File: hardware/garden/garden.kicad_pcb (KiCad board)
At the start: 4 copper layers, 53.3 x 83.8 mm, 53 parts, among them J1 CONN_01X40, J2 CONN_01X08, J3 CONN_01X06, J4 CONN_01X10, J5 CONN_01X08, J7 Micro_SD_Card_CD, J8 CONN_01X13, J9 CONN_01X06, M1 ESP-11, M2 CONN_01X01, M3 CONN_01X01, M4 CONN_01X01, M5 CONN_01X01, P1 USB_OTG, Q1 Q_NMOS_GSD, SW1 RESET, SW2 BOOT, U1 AZ1117-3.3, U2 STM32F745ZETx, U3 IS42S16160G, Y1 12MHz

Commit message: Designed garden controller
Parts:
- added C17: 1uF, Capacitor_SMD:C_0805_2012Metric_Pad1.15x1.40mm_HandSolder, F.Cu at (122.0, 98.0)
- added C18: 0.1uF, Capacitor_SMD:C_0805_2012Metric_Pad1.15x1.40mm_HandSolder, F.Cu at (118.9, 106.0)
- added C19: 0.1uF, Capacitor_SMD:C_0805_2012Metric_Pad1.15x1.40mm_HandSolder, F.Cu at (118.7, 111.1)
- added C20: 0.1uF, Capacitor_SMD:C_0805_2012Metric_Pad1.15x1.40mm_HandSolder, F.Cu at (118.6, 117.5)
- added C21: 220uF, Capacitor_THT:CP_Radial_D8.0mm_P3.50mm, F.Cu at (137.6, 77.7)
- added C22: 220uF, Capacitor_THT:CP_Radial_D8.0mm_P3.50mm, F.Cu at (114.0, 136.0)
- added C23: 22uF, Capacitor_THT:CP_Radial_D6.3mm_P2.50mm, F.Cu at (75.3, 68.3)
- added D7: D_Schottky, Diode_SMD:D_1206_3216Metric_Pad1.42x1.75mm_HandSolder, F.Cu at (147.8, 66.0)
- added J10: CONN_01X10, Connector_PinHeader_2.54mm:PinHeader_1x10_P2.54mm_Vertical, F.Cu at (61.8, 104.6)
- added J6: CONN_01X02, TerminalBlock_Phoenix:TerminalBlock_Phoenix_MKDS-3-2-5.08_1x02_P5.08mm_Horizontal, F.Cu at (148.0, 126.2)
- added Q2: Q_NMOS_GDS, Package_TO_SOT_THT:TO-220-3_Vertical, F.Cu at (128.7, 101.8)
- added Q3: Q_NMOS_GDS, Package_TO_SOT_THT:TO-220-3_Vertical, F.Cu at (128.7, 107.1)
- added R11: 1kR, Resistor_SMD:R_0805_2012Metric_Pad1.15x1.40mm_HandSolder, F.Cu at (94.2, 110.7)
- added R12: 1kR, Resistor_SMD:R_0805_2012Metric_Pad1.15x1.40mm_HandSolder, F.Cu at (94.2, 114.4)
- added U4: MIC4427, Package_SO:SOIC-8_3.9x4.9mm_P1.27mm, F.Cu at (122.0, 93.5)
- added U5: INA193, Package_TO_SOT_SMD:SOT-23-5, F.Cu at (121.9, 106.1)
- added U6: INA193, Package_TO_SOT_SMD:SOT-23-5, F.Cu at (121.9, 111.1)
- added U7: TEC2-1215WI, Converter_DCDC:Converter_DCDC_TRACO_TMR-xxxx_THT, F.Cu at (126.2, 143.7)
- added U8: INA193, Package_TO_SOT_SMD:SOT-23-5, F.Cu at (121.9, 117.4)
- C14: footprint Capacitors_SMD:C_0805 -> Capacitor_SMD:C_0805_2012Metric_Pad1.15x1.40mm_HandSolder
- C15, C16: value 10uF -> 0.1uF; footprint Capacitors_SMD:C_0805 -> Capacitor_SMD:C_0805_2012Metric_Pad1.15x1.40mm_HandSolder
- J1: value CONN_01X40 -> CONN_01X04; footprint ER-CON40HB-2:ER-CON40HB-2 -> Connector_JST:JST_PH_B4B-PH-SM4-TB_1x04-1MP_P2.00mm_Vertical
- J2, J5: value CONN_01X08 -> CONN_01X02; footprint Pin_Headers:Pin_Header_Straight_1x08_Pitch2.54mm -> TerminalBlock_Phoenix:TerminalBlock_Phoenix_MKDS-3-2-5.08_1x02_P5.08mm_Horizontal
- J3: value CONN_01X06 -> CONN_01X04; footprint Pin_Headers:Pin_Header_Straight_1x06_Pitch2.54mm -> Connector_JST:JST_PH_B4B-PH-SM4-TB_1x04-1MP_P2.00mm_Vertical
- J4: value CONN_01X10 -> CONN_01X02; footprint Connector_PinHeader_2.54mm:PinHeader_1x10_P2.54mm_Vertical -> TerminalBlock_Phoenix:TerminalBlock_Phoenix_MKDS-3-2-5.08_1x02_P5.08mm_Horizontal
- J7: value Micro_SD_Card_CD -> CONN_01X04; footprint Amphenol:Amphenol_1140084168 -> TerminalBlock_Phoenix:TerminalBlock_Phoenix_MPT-0,5-4-2.54_1x04_P2.54mm_Horizontal
- J8: value CONN_01X13 -> CONN_01X04; footprint Pin_Headers:Pin_Header_Straight_1x13_Pitch2.54mm -> TerminalBlock_Phoenix:TerminalBlock_Phoenix_MPT-0,5-4-2.54_1x04_P2.54mm_Horizontal
- M2, M3, M4, M5: footprint Mechanical:M2_HOLE -> MountingHole:MountingHole_6.4mm_M6
- R1, R4: value 10KR -> 10mR; footprint Resistors_SMD:R_0805 -> Resistor_SMD:R_1206_3216Metric_Pad1.42x1.75mm_HandSolder
- R5: value 10KR -> 1kR; footprint Resistors_SMD:R_0805 -> Resistor_SMD:R_0805_2012Metric_Pad1.15x1.40mm_HandSolder
- R6: value 10KR -> 6.8R; footprint Resistors_SMD:R_0805 -> Resistor_SMD:R_0805_2012Metric_Pad1.15x1.40mm_HandSolder
- U1: footprint SOT-223 -> Package_TO_SOT_SMD:SOT-223
- U3: value IS42S16160G -> R-78B5.0-2.0; footprint TSOPII:TSOPII-54_10.16x22.22mm-Pitch0.8mm -> Converter_DCDC:Converter_DCDC_RECOM_R-78B-2.0_THT
- moved J1 85.4 mm to (78.4, 82.7), turned to 90 degrees
- moved J7 70.5 mm to (87.0, 144.5), turned to 0 degrees
- moved C14 60.9 mm to (106.4, 76.2)
- moved U3 54.5 mm to (150.4, 75.9), turned to 180 degrees
- moved J3 50.6 mm to (65.5, 82.7), turned to 90 degrees
- moved J2 49.6 mm to (148.0, 82.7), turned to 270 degrees
- moved R6 49.6 mm to (147.8, 122.0)
- moved R1 43.0 mm to (147.4, 92.5)
- moved C15 40.2 mm to (94.2, 105.7)
- moved M2 38.5 mm to (63.8, 56.6)
- moved M5 37.6 mm to (63.2, 141.9)
- moved J8 36.6 mm to (73.9, 144.5), turned to 0 degrees
- moved Q1 34.8 mm to (115.3, 65.7), turned to 90 degrees
- moved P1 30.3 mm to (132.8, 52.3), turned to 270 degrees
- moved C3 29.9 mm to (81.9, 99.3), turned to 90 degrees
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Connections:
- net /PA9 renamed /Vusb
- C16 pad 1: +3V3 -> +12V
- J1 pad 2: /LCD_BL -> /VD_RX
- J1 pad 3: GND -> /VD_TX
- J1 pad 4: /TOUCH_WAKE -> (no net)
- J2 pad 1: Net-(J2-Pad1) -> +12V
- J2 pad 2: +3V3 -> GND
- J3 pad 1: /PA0 -> GND
- J3 pad 2: /PA1 -> /VD_TX
- J3 pad 3: /PA2 -> /VD_RX
- J3 pad 4: /PA3 -> (no net)
- J4 pad 1: /PA8 -> Net-(J4-Pad1)
- J4 pad 2: /PC9 -> Net-(J4-Pad2)
- J5 pad 1: /PG7 -> Net-(J5-Pad1)
- J5 pad 2: /PC6 -> Net-(J5-Pad2)
- J7 pad 1: Net-(J7-Pad1) -> +3V3
- J7 pad 2: /SD_CS -> /SDA
- J7 pad 3: /SD_MOSI -> /SCL
- J7 pad 4: +3V3 -> GND
- J8 pad 2: GND -> /SDA
- J8 pad 3: /~LCD_CS -> /SCL
- J8 pad 4: /~LCD_RD -> GND
- M2 pad 1: Net-(M2-Pad1) -> (no net)
- M3 pad 1: Net-(M3-Pad1) -> (no net)
- M4 pad 1: Net-(M4-Pad1) -> (no net)
- M5 pad 1: Net-(M5-Pad1) -> (no net)
- P1 pad 4: Net-(P1-Pad4) -> (no net)
- R1 pad 1: +3V3 -> +12V
- R1 pad 2: /SD_CD -> Net-(J4-Pad1)
- R4 pad 1: +3V3 -> +12V
- R4 pad 2: /TOUCH_SDA -> Net-(J5-Pad1)
- R5 pad 1: +3V3 -> Net-(R5-Pad1)
- R5 pad 2: /TOUCH_SCL -> /PRESSURE_PWR
- R6 pad 1: +3V3 -> Net-(J6-Pad1)
- R6 pad 2: /SD_MISO -> Net-(R6-Pad2)
- U2 pad 1: /SD_SCLK -> (no net)
- U2 pad 10: /A0 -> /PF0
- U2 pad 100: /PA8 -> (no net)
- U2 pad 102: /PA10 -> (no net)
- U2 pad 11: /A1 -> /PF1
- U2 pad 110: /PA15 -> (no net)
- U2 pad 111: /PC10 -> (no net)
- U2 pad 112: /PC11 -> (no net)
- U2 pad 113: /PC12 -> (no net)
- U2 pad 114: /D2 -> (no net)
- U2 pad 115: /D3 -> (no net)
- U2 pad 116: Net-(U2-Pad116) -> (no net)
- U2 pad 117: Net-(U2-Pad117) -> (no net)
- U2 pad 118: /~LCD_RD -> (no net)
- U2 pad 119: /~LCD_WR -> (no net)
- U2 pad 12: /A2 -> /PF2
- U2 pad 122: /LCD_TE -> (no net)
- U2 pad 123: /~LCD_CS -> (no net)
- U2 pad 13: /A3 -> (no net)
- U2 pad 132: /SDNCAS -> (no net)
- U2 pad 139: Net-(U2-Pad139) -> (no net)
- U2 pad 14: /A4 -> (no net)
- U2 pad 140: Net-(U2-Pad140) -> (no net)
- U2 pad 141: /NBL0 -> /VD_RX
- U2 pad 142: /NBL1 -> /VD_TX
- U2 pad 15: /A5 -> (no net)
- U2 pad 18: Net-(U2-Pad18) -> (no net)
- U2 pad 19: Net-(U2-Pad19) -> (no net)
- U2 pad 2: /SD_CD -> (no net)
- U2 pad 20: Net-(U2-Pad20) -> (no net)
- U2 pad 21: Net-(U2-Pad21) -> (no net)
- U2 pad 22: Net-(U2-Pad22) -> (no net)
- U2 pad 26: /SDNWE -> (no net)
- U2 pad 27: Net-(U2-Pad27) -> (no net)
- U2 pad 28: /SDNE0 -> (no net)
- U2 pad 29: /SDCKE0 -> (no net)
- U2 pad 3: /SD_CS -> (no net)
- U2 pad 34: /PA0 -> (no net)
- U2 pad 4: /SD_MISO -> (no net)
- U2 pad 40: /PA4 -> (no net)
- U2 pad 41: /PA5 -> (no net)
- U2 pad 42: Net-(U2-Pad42) -> (no net)
- U2 pad 43: /PA7 -> (no net)
- U2 pad 44: Net-(U2-Pad44) -> (no net)
- U2 pad 45: Net-(U2-Pad45) -> /PRESSURE_CUR
- U2 pad 46: Net-(U2-Pad46) -> /SW1_CUR
- U2 pad 47: Net-(U2-Pad47) -> /SW0_CUR
- U2 pad 48: Net-(U2-Pad48) -> (no net)
- U2 pad 49: /SDNRAS -> (no net)
- U2 pad 5: /SD_MOSI -> (no net)
- U2 pad 50: /A6 -> (no net)
- U2 pad 53: /A7 -> (no net)
- U2 pad 54: /A8 -> /SCL
- U2 pad 55: /A9 -> /SDA
- U2 pad 56: /A10 -> (no net)
- U2 pad 57: /A11 -> (no net)
- U2 pad 58: /D4 -> (no net)
- U2 pad 59: /D5 -> (no net)
- U2 pad 60: /D6 -> (no net)
- U2 pad 63: /D7 -> (no net)
- U2 pad 64: /D8 -> (no net)
- U2 pad 65: /D9 -> (no net)
- U2 pad 66: /D10 -> (no net)
- U2 pad 67: /D11 -> (no net)
- U2 pad 68: /D12 -> (no net)
- U2 pad 69: /TOUCH_SCL -> (no net)
- U2 pad 7: Net-(U2-Pad7) -> (no net)
- U2 pad 70: /TOUCH_SDA -> /PRESSURE_PWR
- U2 pad 73: /TOUCH_INT -> (no net)
- U2 pad 74: /TOUCH_WAKE -> (no net)
- U2 pad 75: /TOUCH_RESET -> (no net)
- U2 pad 76: /LCD_BL -> (no net)
- U2 pad 77: /D13 -> (no net)
- U2 pad 78: /D14 -> (no net)
- U2 pad 79: /D15 -> (no net)
- U2 pad 8: Net-(U2-Pad8) -> (no net)
- U2 pad 80: /PD11 -> (no net)
- U2 pad 81: /PD12 -> (no net)
- U2 pad 82: /PD13 -> (no net)
- U2 pad 85: /D0 -> (no net)
- U2 pad 86: /D1 -> (no net)
- U2 pad 87: /A12 -> (no net)
- U2 pad 88: Net-(U2-Pad88) -> (no net)
- U2 pad 89: /BA0 -> (no net)
- U2 pad 9: Net-(U2-Pad9) -> (no net)
- U2 pad 90: /BA1 -> (no net)
- U2 pad 91: /PG6 -> (no net)
- U2 pad 92: /PG7 -> /SW1_SIG
- U2 pad 93: /SDCLK -> /SW0_SIG
- U2 pad 96: /PC6 -> (no net)
- U2 pad 97: /PC7 -> (no net)
- U2 pad 98: /PC8 -> (no net)
- U2 pad 99: /PC9 -> (no net)
- U3 pad 1: +3V3 -> +12V
- U3 pad 2: /D0 -> GND
- U3 pad 3: +3V3 -> Net-(D7-Pad2)
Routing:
- net +3V3: track 159.8 -> 354.3 mm, vias 33 -> 16
- net GND: track 145.8 -> 297.4 mm, vias 41 -> 34
- net +12V: track 0.00 -> 126.2 mm, vias 0 -> 10
- net VCC: track 116.1 -> 11.7 mm, vias 1 -> 0
- net /~LCD_RD: track 74.5 -> 0.00 mm, vias 4 -> 0
- net /~LCD_WR: track 74.3 -> 0.00 mm, vias 4 -> 0
- net /LCD_TE: track 74.2 -> 0.00 mm, vias 4 -> 0
- net /~LCD_CS: track 73.3 -> 0.00 mm, vias 4 -> 0
- net /SCL: track 0.00 -> 72.5 mm, vias 0 -> 2
- net /SDA: track 0.00 -> 70.1 mm, vias 0 -> 5
- net /D2: track 62.1 -> 0.00 mm, vias 4 -> 0
- net /D3: track 60.2 -> 0.00 mm, vias 4 -> 0
- net /TOUCH_SCL: track 58.1 -> 0.00 mm, vias 2 -> 0
- net /TOUCH_SDA: track 57.6 -> 0.00 mm, vias 2 -> 0
- net /D0: track 52.2 -> 0.00 mm, vias 4 -> 0
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- added copper zone on B.Cu, net +12V
- added copper zone on B.Cu, net +3V3
- added copper zone on B.Cu, net GND
- removed copper zone on F.Cu, net +3V3
- removed copper zone on VDD, net +3V3
- removed copper zone on GND, net GND
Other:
- board size 53.3 x 83.8 mm -> 99.7 x 99.7 mm
- copper layers 4 -> 2
- rule via_min_size: 0.4 -> 0.45
- board text added: "+"
- board text added: "-"
- board text added: "12V"
- board text added: "I2C0"
- board text added: "I2C1"
- board text added: "PA1"
- board text added: "PA2"
- board text added: "PA3"
- board text added: "PF0"
- board text added: "PF1"
- board text added: "PF2"
- board text added: "Pressure IN"
- board text added: "Pump OUT"
- board text added: "SCL"
- board text added: "SDA"
- board text added: "SW1 OUT"
- board text added: "Solar Power IN"
- board text added: "VE.Direct"
- board text added: "WiredHut Garden Controller Rev 1"
- board text removed: "A0"
- board text removed: "A1"
- board text removed: "A2"
- board text removed: "A3"
- board text removed: "A4"
- board text removed: "A5"
- board text removed: "D0"
- board text removed: "D1"
- board text removed: "D10"
- board text removed: "D11"
- board text removed: "D12"
- board text removed: "D13"
- board text removed: "D14"
- board text removed: "D15"
- board text removed: "D2"
- board text removed: "D20"
- board text removed: "D21"
- board text removed: "D22"
- board text removed: "D23"
- board text removed: "D24"
- board text removed: "D25"
- board text removed: "D26"
- board text removed: "D27"
- board text removed: "D28"
- board text removed: "D3"
- board text removed: "D4"
- board text removed: "D5"
- board text removed: "D6"
- board text removed: "D7"
- board text removed: "D8"
- board text removed: "D9"
- board text removed: "Ostrich"
- board text removed: "Rev 2"
- board text removed: "VCC"
- board text removed: "Vcc"
- board text removed: "~RST"

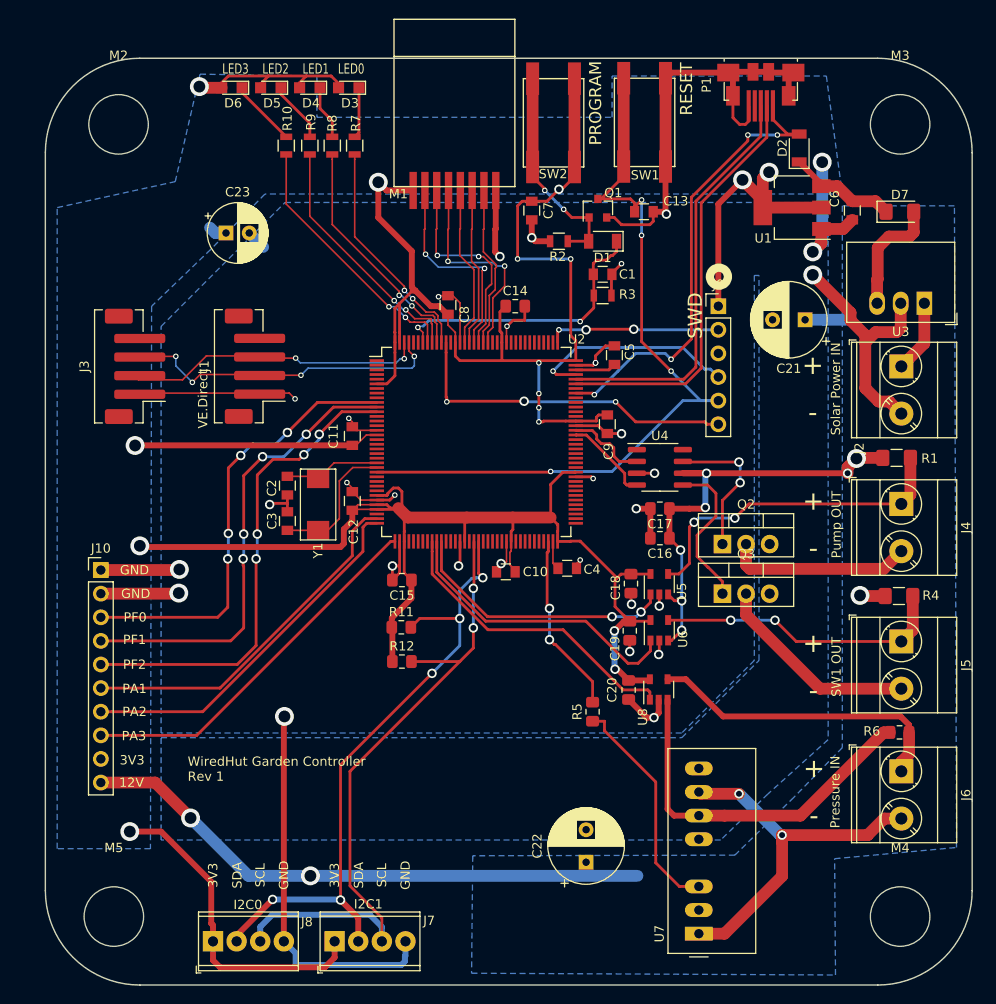
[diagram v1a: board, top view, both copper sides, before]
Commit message: Updated garden controller with test points and back emf diodes
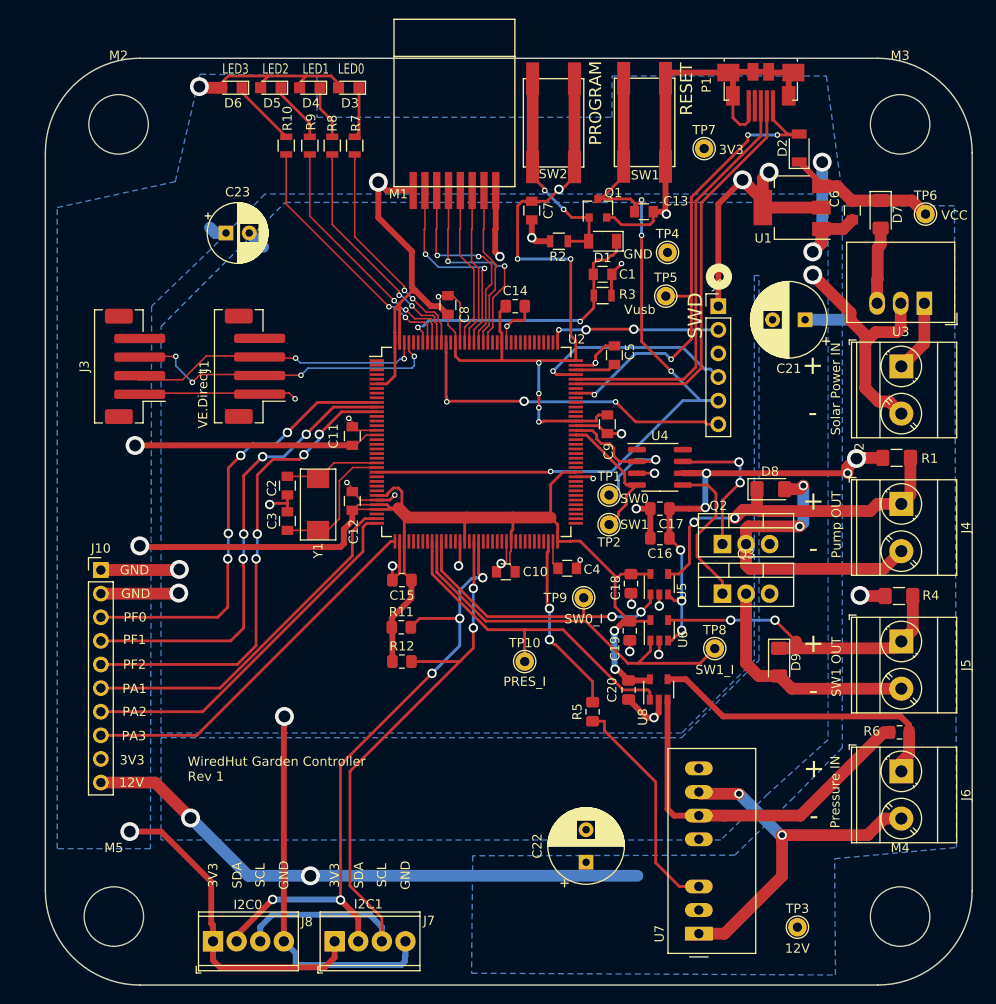
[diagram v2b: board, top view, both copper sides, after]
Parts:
- added D8: D_Schottky, Diode_SMD:D_1206_3216Metric_Pad1.42x1.75mm_HandSolder, F.Cu at (133.9, 95.9)
- added D9: D_Schottky, Diode_SMD:D_1206_3216Metric_Pad1.42x1.75mm_HandSolder, F.Cu at (134.8, 114.5)
- added TP1: TestPoint, TestPoint:TestPoint_THTPad_D2.0mm_Drill1.0mm, F.Cu at (116.5, 96.5)
- added TP10: TestPoint, TestPoint:TestPoint_THTPad_D2.0mm_Drill1.0mm, F.Cu at (107.4, 114.4)
- added TP2: TestPoint, TestPoint:TestPoint_THTPad_D2.0mm_Drill1.0mm, F.Cu at (116.5, 99.7)
- added TP3: TestPoint, TestPoint:TestPoint_THTPad_D2.0mm_Drill1.0mm, F.Cu at (136.8, 143.0)
- added TP4: TestPoint, TestPoint:TestPoint_THTPad_D2.0mm_Drill1.0mm, F.Cu at (122.8, 70.4)
- added TP5: TestPoint, TestPoint:TestPoint_THTPad_D2.0mm_Drill1.0mm, F.Cu at (122.6, 75.1)
- added TP6: TestPoint, TestPoint:TestPoint_THTPad_D2.0mm_Drill1.0mm, F.Cu at (150.6, 66.3)
- added TP7: TestPoint, TestPoint:TestPoint_THTPad_D2.0mm_Drill1.0mm, F.Cu at (126.7, 59.2)
- added TP8: TestPoint, TestPoint:TestPoint_THTPad_D2.0mm_Drill1.0mm, F.Cu at (127.9, 113.0)
- added TP9: TestPoint, TestPoint:TestPoint_THTPad_D2.0mm_Drill1.0mm, F.Cu at (113.8, 107.6)
- moved D7 2.09 mm to (145.7, 66.3), turned to 270 degrees
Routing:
- net Net-(D8-Pad2): track 19.9 -> 34.2 mm, vias 0 -> 2
- net /SW0_SIG: track 8.74 -> 18.3 mm, vias 0 -> 1
- net /SW1_CUR: track 32.0 -> 40.9 mm
- net /SW1_SIG: track 9.41 -> 14.9 mm
- net Net-(D7-Pad2): track 12.8 -> 8.23 mm
- net VCC: track 11.7 -> 16.1 mm
- net /PRESSURE_CUR: track 33.0 -> 36.4 mm
- net Net-(D9-Pad2): track 22.3 -> 25.3 mm
- net Net-(D9-Pad1): track 31.4 -> 34.4 mm
- net /Vusb: track 50.5 -> 53.3 mm
- net Net-(D8-Pad1): track 35.9 -> 38.2 mm
- net /SW0_CUR: track 29.2 -> 31.3 mm
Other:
- board text added: "PRES_I"
- board text added: "SW0"
- board text added: "SW0_I"
- board text added: "SW1"
- board text added: "SW1_I"
- board text added: "VCC"
- board text added: "Vusb"

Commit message: Cosmetic changes and added fab files
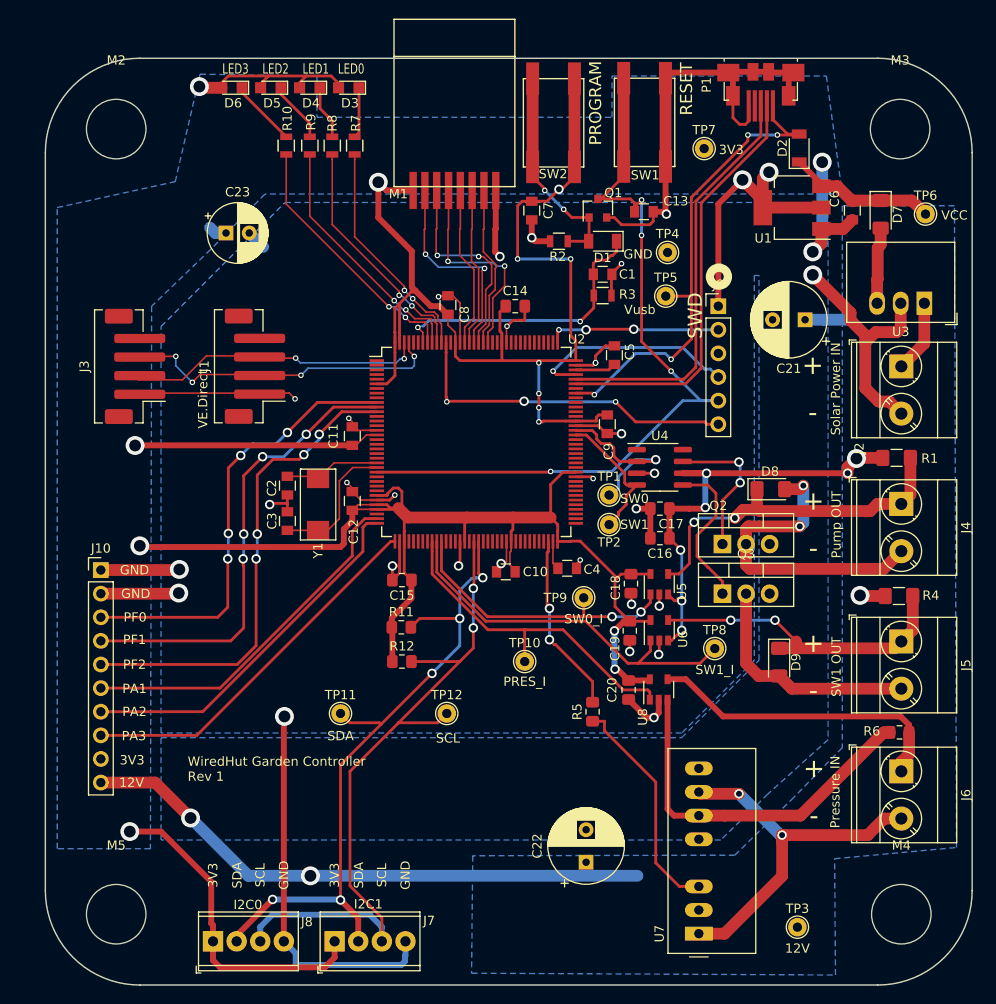
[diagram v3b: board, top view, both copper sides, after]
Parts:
- added TP11: TestPoint, TestPoint:TestPoint_THTPad_D2.0mm_Drill1.0mm, F.Cu at (87.6, 120.0)
- added TP12: TestPoint, TestPoint:TestPoint_THTPad_D2.0mm_Drill1.0mm, F.Cu at (99.1, 120.0)
- moved M2 0.57 mm to (63.5, 57.1)
- moved M3 0.51 mm to (147.8, 57.1)
- moved M5 0.36 mm to (63.5, 141.6)
- moved M4 0.28 mm to (148.0, 141.6)
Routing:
- net /SCL: track 72.5 -> 78.1 mm
- net /SDA: track 70.1 -> 74.9 mm

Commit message: Added second gen garden board
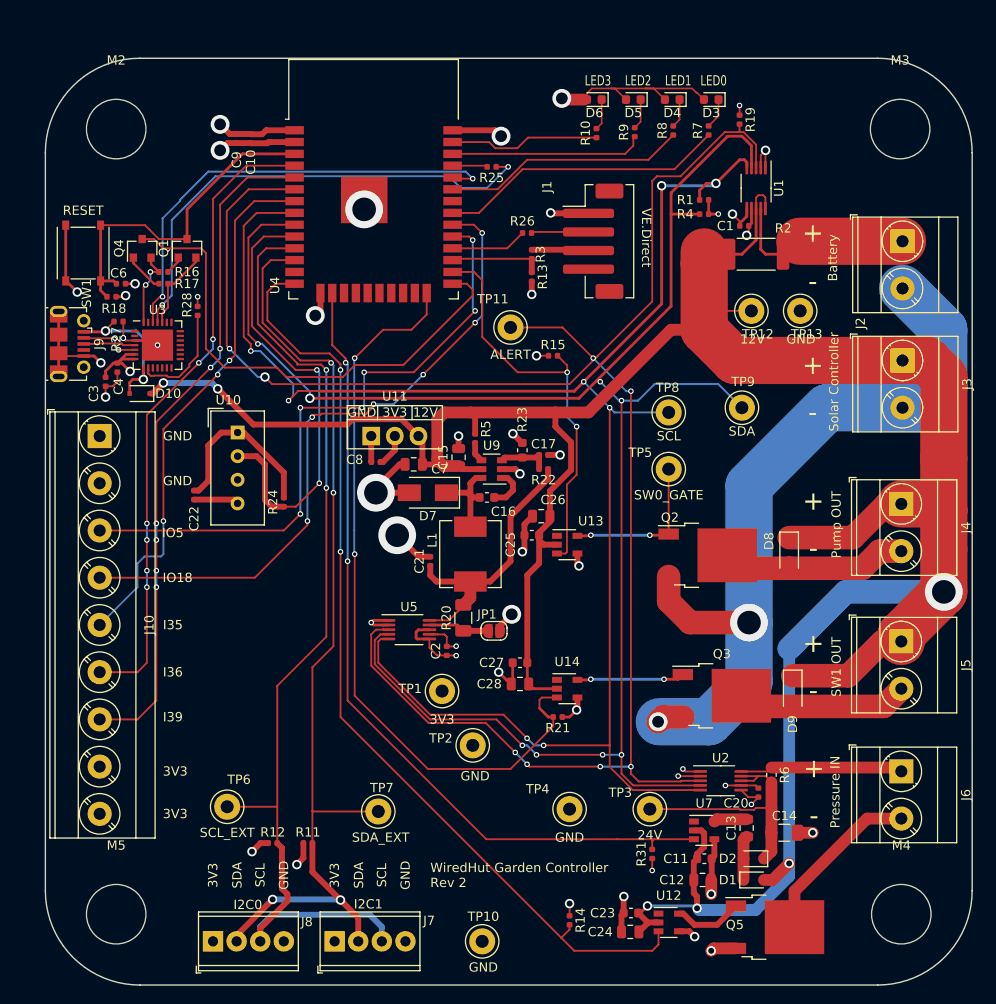
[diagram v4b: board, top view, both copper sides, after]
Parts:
- removed C18, C19: 0.1uF, Capacitor_SMD:C_0805_2012Metric_Pad1.15x1.40mm_HandSolder
- removed C5: 22uF, Capacitors_SMD:C_0805
- removed M1: ESP-11, ESP-11:ESP-11
- removed P1: USB_OTG, USB:USB_Micro-B_Molex_47346-0001_HS
- removed SW2: BOOT, LL3301NF065QG:LL3301NF065QG
- removed U6, U8: INA193, Package_TO_SOT_SMD:SOT-23-5
- removed Y1: 12MHz, Crystals:Crystal_SMD_Abracon_ABM3-2pin_5.0x3.2mm_HandSoldering
- added C24: 1uF/50V, Capacitor_SMD:C_0805_2012Metric, F.Cu at (118.8, 143.5)
- added C25: 0.1uF/50V, Capacitor_SMD:C_0603_1608Metric, F.Cu at (108.2, 100.8)
- added C26: 1uF/50V, Capacitor_SMD:C_0805_2012Metric, F.Cu at (109.2, 98.8)
- added C27: 0.1uF/50V, Capacitor_SMD:C_0603_1608Metric, F.Cu at (106.9, 114.6)
- added C28: 1uF/50V, Capacitor_SMD:C_0805_2012Metric, F.Cu at (106.9, 116.8)
- added D10: D, Diode_SMD:D_SOD-323F, F.Cu at (66.0, 85.6)
- added JP1: Jumper, Jumper:SolderJumper-2_P1.3mm_Open_RoundedPad1.0x1.5mm, F.Cu at (104.1, 111.1)
- added L1: 4.7uH, MWSA0603:MWSA0603, F.Cu at (101.6, 102.9)
- added Q4: Q_NPN_BEC, Package_TO_SOT_SMD:SOT-23, F.Cu at (66.3, 70.0)
- added Q5: Q_NMOS_GDS, Package_TO_SOT_SMD:TO-252-2, F.Cu at (134.4, 143.0)
- added R13: 2kR, Resistor_SMD:R_0402_1005Metric, F.Cu at (108.2, 73.0)
- added R14: 10kR, Resistor_SMD:R_0402_1005Metric, F.Cu at (112.3, 142.3)
- added R15: 10kR, Resistor_SMD:R_0402_1005Metric, F.Cu at (110.5, 81.5)
- added R16: 10kR, Resistor_SMD:R_0402_1005Metric, F.Cu at (68.6, 72.5)
- added R17: 10kR, Resistor_SMD:R_0402_1005Metric, F.Cu at (68.6, 73.8)
- added R18: 10kR, Resistor_SMD:R_0402_1005Metric, F.Cu at (63.0, 75.2)
- added R19: 2.2kR, Resistor_SMD:R_0402_1005Metric, F.Cu at (130.6, 56.1)
- added R20: 0.1R, Resistor_SMD:R_1206_3216Metric, F.Cu at (100.8, 109.7)
- added R21: 10kR, Resistor_SMD:R_0402_1005Metric, F.Cu at (111.0, 120.4)
- added R22: 124kR, Resistor_SMD:R_0402_1005Metric, F.Cu at (109.5, 93.7)
- added R23: 40.2kR, Resistor_SMD:R_0603_1608Metric, F.Cu at (107.2, 91.7)
- added R24: 10kR, Resistor_SMD:R_0402_1005Metric, F.Cu at (81.5, 97.3)
- added R25: 470R, Resistor_SMD:R_0402_1005Metric, F.Cu at (103.9, 61.2)
- added R26: 470R, Resistor_SMD:R_0402_1005Metric, F.Cu at (107.7, 68.3)
- added R27: 10kR, Resistor_SMD:R_0402_1005Metric, F.Cu at (63.8, 77.9)
- added R28: 10kR, Resistor_SMD:R_0402_1005Metric, F.Cu at (72.3, 76.7)
- added R31: 10kR, Resistor_SMD:R_0402_1005Metric, F.Cu at (121.2, 135.1)
- added TP13: TestPoint, TestPoint:TestPoint_Loop_D3.50mm_Drill1.4mm_Beaded, F.Cu at (137.1, 76.7)
- added U10: DHT11, Sensor:Aosong_DHT11_5.5x12.0_P2.54mm, F.Cu at (76.6, 89.8)
- added U11: AZ1117-3.3, Package_TO_SOT_THT:TO-220-3_Vertical, F.Cu at (90.9, 90.2)
- added U12: MCP1416, Package_TO_SOT_SMD:SOT-23-5, F.Cu at (122.9, 142.5)
- added U13: MCP1416, Package_TO_SOT_SMD:SOT-23-5, F.Cu at (112.0, 101.9)
- added U14: MCP1416, Package_TO_SOT_SMD:SOT-23-5, F.Cu at (112.0, 117.3)
- added U9: MP2451DT, Package_TO_SOT_SMD:SOT-23-6, F.Cu at (103.9, 93.7)
- C1: value 1uF -> 0.1uF; footprint Capacitors_SMD:C_0805 -> Capacitor_SMD:C_0402_1005Metric
- C10: footprint Capacitors_SMD:C_0805 -> Capacitor_SMD:C_0402_1005Metric
- C11: value 0.1uF -> 0.1uF/50V; footprint Capacitors_SMD:C_0805 -> Capacitor_SMD:C_0603_1608Metric
- C12, C13: value 0.1uF -> 1uF/50V; footprint Capacitors_SMD:C_0805 -> Capacitor_SMD:C_0805_2012Metric
- C14: value 0.1uF -> 10uF/50V; footprint Capacitor_SMD:C_0805_2012Metric_Pad1.15x1.40mm_HandSolder -> Capacitor_SMD:C_1206_3216Metric
- C15: value 0.1uF -> 22uF; footprint Capacitor_SMD:C_0805_2012Metric_Pad1.15x1.40mm_HandSolder -> Capacitor_SMD:C_0805_2012Metric
- C16: value 0.1uF -> 0.1uF/50V; footprint Capacitor_SMD:C_0805_2012Metric_Pad1.15x1.40mm_HandSolder -> Capacitor_SMD:C_0603_1608Metric
- C17: value 1uF -> 33pF; footprint Capacitor_SMD:C_0805_2012Metric_Pad1.15x1.40mm_HandSolder -> Capacitor_SMD:C_0402_1005Metric
- C2: value 16pF -> 0.1uF; footprint Capacitors_SMD:C_0805 -> Capacitor_SMD:C_0402_1005Metric
- C20: footprint Capacitor_SMD:C_0805_2012Metric_Pad1.15x1.40mm_HandSolder -> Capacitor_SMD:C_0402_1005Metric
- C21: value 220uF -> 10uF; footprint Capacitor_THT:CP_Radial_D8.0mm_P3.50mm -> Capacitor_SMD:C_0402_1005Metric
- C22: value 220uF -> 0.1uF; footprint Capacitor_THT:CP_Radial_D8.0mm_P3.50mm -> Capacitor_SMD:C_0402_1005Metric
- C23: value 22uF -> 0.1uF/50V; footprint Capacitor_THT:CP_Radial_D6.3mm_P2.50mm -> Capacitor_SMD:C_0603_1608Metric
- C3: value 16pF -> 1uF; footprint Capacitors_SMD:C_0805 -> Capacitor_SMD:C_0402_1005Metric
- C4: value 22uF -> 0.1uF; footprint Capacitors_SMD:C_0805 -> Capacitor_SMD:C_0402_1005Metric
- C6: value 10uF -> 0.1uF; footprint Capacitors_SMD:C_0805 -> Capacitor_SMD:C_0402_1005Metric
- C7: value 10uF -> 22uF; footprint Capacitors_SMD:C_0805 -> Capacitor_SMD:C_0805_2012Metric
- C8, C9: value 0.1uF -> 10uF; footprint Capacitors_SMD:C_0805 -> Capacitor_SMD:C_0402_1005Metric
- D1, D2: value D_Schottky -> D; footprint Diodes_SMD:D_1206 -> Diode_SMD:D_SOD-323F
- D3, D5: value LED -> GREEN; footprint LEDs:LED_0805 -> LED_SMD:LED_0603_1608Metric
- D4, D6: value LED -> RED; footprint LEDs:LED_0805 -> LED_SMD:LED_0603_1608Metric
- D7: footprint Diode_SMD:D_1206_3216Metric_Pad1.42x1.75mm_HandSolder -> Diode_SMD:D_SMA
- D8, D9: footprint Diode_SMD:D_1206_3216Metric_Pad1.42x1.75mm_HandSolder -> Diode_SMD:D_SOD-123
- J10: value CONN_01X10 -> CONN_01X09; footprint Connector_PinHeader_2.54mm:PinHeader_1x10_P2.54mm_Vertical -> TerminalBlock_Phoenix:TerminalBlock_Phoenix_MKDS-3-9-5.08_1x09_P5.08mm_Horizontal
- J3: value CONN_01X04 -> CONN_01X02; footprint Connector_JST:JST_PH_B4B-PH-SM4-TB_1x04-1MP_P2.00mm_Vertical -> TerminalBlock_Phoenix:TerminalBlock_Phoenix_MKDS-3-2-5.08_1x02_P5.08mm_Horizontal
- J9: value CONN_01X06 -> USB_B_Micro; footprint Connector_PinHeader_2.54mm:PinHeader_1x06_P2.54mm_Vertical -> Connector_USB:USB_Micro-B_Molex-105017-0001
- Q1: value Q_NMOS_GSD -> Q_NPN_BEC; footprint TO_SOT_Packages_SMD:SOT-23 -> Package_TO_SOT_SMD:SOT-23
- Q2, Q3: footprint Package_TO_SOT_THT:TO-220-3_Vertical -> Package_TO_SOT_SMD:TO-252-2
- R1, R4: value 10mR -> 2.2kR; footprint Resistor_SMD:R_1206_3216Metric_Pad1.42x1.75mm_HandSolder -> Resistor_SMD:R_0402_1005Metric
- R10, R7, R8, R9: footprint Resistors_SMD:R_0805 -> Resistor_SMD:R_0402_1005Metric
- R11, R12: footprint Resistor_SMD:R_0805_2012Metric_Pad1.15x1.40mm_HandSolder -> Resistor_SMD:R_0402_1005Metric
- R2: value 1KR -> 12mR; footprint Resistors_SMD:R_0805 -> Resistor_SMD:R_2512_6332Metric
- R3: value 1MR -> 1kR; footprint Resistors_SMD:R_0805 -> Resistor_SMD:R_0402_1005Metric
- R5: value 1kR -> 100kR; footprint Resistor_SMD:R_0805_2012Metric_Pad1.15x1.40mm_HandSolder -> Resistor_SMD:R_0402_1005Metric
- R6: value 6.8R -> 2.2R; footprint Resistor_SMD:R_0805_2012Metric_Pad1.15x1.40mm_HandSolder -> Resistor_SMD:R_0603_1608Metric
- SW1: value RESET -> SW_Push; footprint LL3301NF065QG:LL3301NF065QG -> Switch:SW_Push_1P1T_NO_5.1x5.1mm
- TP1, TP10, TP11, TP12, TP2, TP3, TP4, TP5, TP6, TP7, TP8, TP9: footprint TestPoint:TestPoint_THTPad_D2.0mm_Drill1.0mm -> TestPoint:TestPoint_Loop_D3.50mm_Drill1.4mm_Beaded
- U1: value AZ1117-3.3 -> INA226; footprint Package_TO_SOT_SMD:SOT-223 -> Package_SO:VSSOP-10_3x3mm_P0.5mm
- U2: value STM32F745ZETx -> INA226; footprint Housings_QFP:LQFP-144_20x20mm_Pitch0.5mm -> Package_SO:VSSOP-10_3x3mm_P0.5mm
- U3: value R-78B5.0-2.0 -> CP2102; footprint Converter_DCDC:Converter_DCDC_RECOM_R-78B-2.0_THT -> Package_DFN_QFN:QFN-28-1EP_5x5mm_P0.5mm_EP3.35x3.35mm
- U4: value MIC4427 -> ESP32-WROOM-32; footprint Package_SO:SOIC-8_3.9x4.9mm_P1.27mm -> RF_Module:ESP32-WROOM-32
- U5: value INA193 -> INA226; footprint Package_TO_SOT_SMD:SOT-23-5 -> Package_SO:VSSOP-10_3x3mm_P0.5mm
- U7: value TEC2-1215WI -> MCP1416; footprint Converter_DCDC:Converter_DCDC_TRACO_TMR-xxxx_THT -> Package_TO_SOT_SMD:SOT-23-5
- moved TP6 98.5 mm to (75.4, 130.0)
- moved C23 85.1 mm to (118.9, 141.5), turned to 180 degrees
- moved U3 82.6 mm to (67.9, 80.4), turned to 0 degrees
- moved J3 82.6 mm to (148.1, 82.0), turned to 270 degrees
- moved TP7 79.5 mm to (91.7, 130.6)
- moved C6 79.1 mm to (64.0, 73.8), turned to 0 degrees
- moved D2 76.6 mm to (132.1, 135.6), turned to 180 degrees
- moved D1 70.6 mm to (132.1, 137.9), turned to 0 degrees
- moved J9 69.8 mm to (58.5, 80.3), turned to 270 degrees
- moved C13 67.2 mm to (131.3, 132.3), turned to 90 degrees
- moved C14 63.6 mm to (135.4, 132.8)
- moved TP4 60.8 mm to (112.3, 130.3)
- moved C11 59.2 mm to (126.8, 135.6), turned to 0 degrees
- moved SW1 58.1 mm to (59.9, 70.5), turned to 270 degrees
- moved C22 57.8 mm to (71.9, 96.5), turned to 270 degrees
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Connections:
- C1 pad 1: /BOOT0 -> +3V3
- C11 pad 1: +3V3 -> +12V
- C12 pad 1: +3V3 -> +12V
- C13 pad 1: /NRST -> Net-(C13-Pad1)
- C13 pad 2: GND -> Net-(C13-Pad2)
- C14 pad 1: +3V3 -> /PRES_SHUNT_P
- C15 pad 1: +3V3 -> +12V
- C16 pad 1: +12V -> Net-(C16-Pad1)
- C16 pad 2: GND -> Net-(C16-Pad2)
- C17 pad 1: +12V -> Net-(C17-Pad1)
- C2 pad 1: Net-(C2-Pad1) -> +3V3
- C21 pad 1: +12V -> /3V3_SHUNT_P
- C22 pad 1: +12V -> +3V3
- C23 pad 1: +3V3 -> +12V
- C3 pad 1: Net-(C3-Pad1) -> +3V3
- C4 pad 1: Net-(C4-Pad1) -> +3V3
- C6 pad 1: VCC -> /EN
- C7 pad 1: +3V3 -> +12V
- D1 pad 1: /BOOT0 -> Net-(C13-Pad1)
- D1 pad 2: Net-(D1-Pad2) -> +12V
- D2 pad 1: VCC -> /PRES_SHUNT_P
- D2 pad 2: /Vusb -> Net-(C13-Pad1)
- D7 pad 1: VCC -> Net-(C16-Pad2)
- D7 pad 2: Net-(D7-Pad2) -> GND
- D8 pad 1: Net-(D8-Pad1) -> +12V
- D9 pad 1: Net-(D9-Pad1) -> +12V
- J1 pad 3: /VD_TX -> Net-(J1-Pad3)
- J10 pad 3: /PF0 -> /IO5
- J10 pad 4: /PF1 -> /IO18
- J10 pad 5: /PF2 -> /I35
- J10 pad 6: /PA1 -> /I36
- J10 pad 7: /PA2 -> /I39
- J10 pad 8: /PA3 -> +3V3
- J2 pad 1: +12V -> /BATT_SHUNT_N
- J3 pad 1: GND -> +12V
- J3 pad 2: /VD_TX -> GND
- J4 pad 1: Net-(D8-Pad1) -> +12V
- J5 pad 1: Net-(D9-Pad1) -> +12V
- J6 pad 1: Net-(J6-Pad1) -> /PRES_SHUNT_N
- J6 pad 2: GND -> Net-(J6-Pad2)
- J7 pad 2: /SDA -> /SDA_EXT
- J7 pad 3: /SCL -> /SCL_EXT
- J8 pad 2: /SDA -> /SDA_EXT
- J8 pad 3: /SCL -> /SCL_EXT
- J9 pad 1: +3V3 -> Net-(D10-Pad2)
- J9 pad 2: /SWCLK -> Net-(J9-Pad2)
- J9 pad 3: GND -> Net-(J9-Pad3)
- J9 pad 4: /SWDIO -> (no net)
- J9 pad 5: /NRST -> GND
- J9 pad 6: /SWO -> GND
- Q1 pad 1: Net-(D1-Pad2) -> Net-(Q1-Pad1)
- Q1 pad 2: GND -> /USB_RTS
- Q1 pad 3: /NRST -> /EN
- R1 pad 1: +12V -> +3V3
- R1 pad 2: Net-(D8-Pad1) -> /SCL
- R10 pad 1: /PB7 -> /LED3
- R11 pad 2: /SDA -> /SDA_EXT
- R12 pad 2: /SCL -> /SCL_EXT
- R2 pad 1: GND -> +12V
- R2 pad 2: Net-(D1-Pad2) -> /BATT_SHUNT_N
- R3 pad 1: /BOOT0 -> Net-(J1-Pad3)
- R3 pad 2: GND -> /VD_TX
- R4 pad 1: +12V -> +3V3
- R4 pad 2: Net-(D9-Pad1) -> /SDA
- R5 pad 1: Net-(R5-Pad1) -> +12V
- R5 pad 2: /PRESSURE_PWR -> Net-(R5-Pad2)
- R6 pad 1: Net-(J6-Pad1) -> /PRES_SHUNT_N
- R6 pad 2: Net-(R6-Pad2) -> /PRES_SHUNT_P
- R7 pad 1: /PB4 -> /LED0
- R8 pad 1: /PB5 -> /LED1
- R9 pad 1: /PB6 -> /LED2
- SW1 pad 1: /NRST -> /EN
- TP1 pad 1: /SW0_SIG -> +3V3
- TP10 pad 1: /PRESSURE_CUR -> GND
- TP11 pad 1: /SDA -> /ALERT
- TP12 pad 1: /SCL -> +12V
- TP2 pad 1: /SW1_SIG -> GND
- TP3 pad 1: +12V -> /PRES_SHUNT_P
- TP5 pad 1: /Vusb -> /SW0_GATE
- TP6 pad 1: VCC -> /SCL_EXT
- TP7 pad 1: +3V3 -> /SDA_EXT
- TP8 pad 1: /SW1_CUR -> /SCL
- TP9 pad 1: /SW0_CUR -> /SDA
- U1 pad 2: +3V3 -> GND
- U1 pad 3: VCC -> /ALERT
- U1 pad 4: +3V3 -> /SDA
- U2 pad 1: (no net) -> +3V3
- U2 pad 10: /PF0 -> /PRES_SHUNT_N
- U2 pad 2: (no net) -> GND
- U2 pad 3: (no net) -> /ALERT
- U2 pad 4: (no net) -> /SDA
- U2 pad 5: (no net) -> /SCL
- U2 pad 7: (no net) -> GND
- U2 pad 8: (no net) -> /PRES_SHUNT_P
- U2 pad 9: (no net) -> /PRES_SHUNT_P
- U3 pad 1: +12V -> (no net)
- U3 pad 2: GND -> (no net)
- U3 pad 3: Net-(D7-Pad2) -> GND
- U4 pad 1: (no net) -> GND
- U4 pad 2: /SW0_SIG -> +3V3
- U4 pad 3: GND -> /EN
- U4 pad 4: /SW1_SIG -> /I36
- U4 pad 5: /SW1_GATE -> /I39
- U4 pad 6: +12V -> /ALERT
- U4 pad 7: /SW0_GATE -> /I35
- U4 pad 8: (no net) -> /SCL
- U5 pad 1: /SW0_CUR -> +3V3
- U5 pad 2: GND -> +3V3
- U5 pad 3: +12V -> /ALERT
- U5 pad 4: Net-(D8-Pad1) -> /SDA
- U5 pad 5: +3V3 -> /SCL
- U7 pad 1: GND -> (no net)
- U7 pad 3: Net-(R5-Pad1) -> /PRESSURE_PWR
- U7 pad 5: (no net) -> Net-(C13-Pad2)
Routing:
- net +3V3: track 354.3 -> 93.1 mm, vias 16 -> 15
- net /ALERT: track 0.00 -> 207.4 mm, vias 0 -> 8
- net +12V: track 126.2 -> 319.0 mm, vias 10 -> 6
- net /SDA: track 74.9 -> 200.3 mm, vias 5 -> 8
- net /SCL: track 78.1 -> 191.1 mm, vias 2 -> 8
- net /SCL_EXT: track 0.00 -> 109.1 mm, vias 0 -> 2
- net /SDA_EXT: track 0.00 -> 104.7 mm, vias 0 -> 4
- net /PRESSURE_SW: track 0.00 -> 102.2 mm, vias 0 -> 2
- net /NRST: track 87.0 -> 0.00 mm, vias 4 -> 0
- net GND: track 297.4 -> 215.6 mm, vias 34 -> 38
- net /SW1: track 0.00 -> 80.6 mm, vias 0 -> 2
- net /I39: track 0.00 -> 72.3 mm, vias 0 -> 6
- net /IO18: track 0.00 -> 71.9 mm, vias 0 -> 6
- net /PRESSURE_PWR: track 19.4 -> 89.1 mm
- net /IO5: track 0.00 -> 69.0 mm, vias 0 -> 6
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- added copper zone on Vcc.Cu, net +3V3
- added copper zone on Gnd.Cu, net GND
- removed copper zone on B.Cu, net +12V
- removed copper zone on B.Cu, net +3V3
- removed copper zone on B.Cu, net GND
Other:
- copper layers 2 -> 4
- net class Antenna feed added: clearance 0.2032, trace_width 0.29337, via_dia 0.6, via_drill 0.35
- rule trace_min: 0.1524 -> 0.0889
- board text added: "24V"
- board text added: "ALERT"
- board text added: "Battery"
- board text added: "I35"
- board text added: "I36"
- board text added: "I39"
- board text added: "IO18"
- board text added: "IO5"
- board text added: "SCL_EXT"
- board text added: "SDA_EXT"
- board text added: "SW0_GATE"
- board text added: "Solar Controller"
- board text added: "WiredHut Garden Controller Rev 2"
- board text removed: "PA1"
- board text removed: "PA2"
- board text removed: "PA3"
- board text removed: "PF0"
- board text removed: "PF1"
- board text removed: "PF2"
- board text removed: "PRES_I"
- board text removed: "PROGRAM"
- board text removed: "SW0"
- board text removed: "SW0_I"
- board text removed: "SW1"
- board text removed: "SW1_I"
- board text removed: "SWD"
- board text removed: "Solar Power IN"
- board text removed: "VCC"
- board text removed: "Vusb"
- board text removed: "WiredHut Garden Controller Rev 1"
